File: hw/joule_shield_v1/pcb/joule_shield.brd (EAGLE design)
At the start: 160 x 100 mm, 18 parts, among them U2 BQ25892PWQFN-24

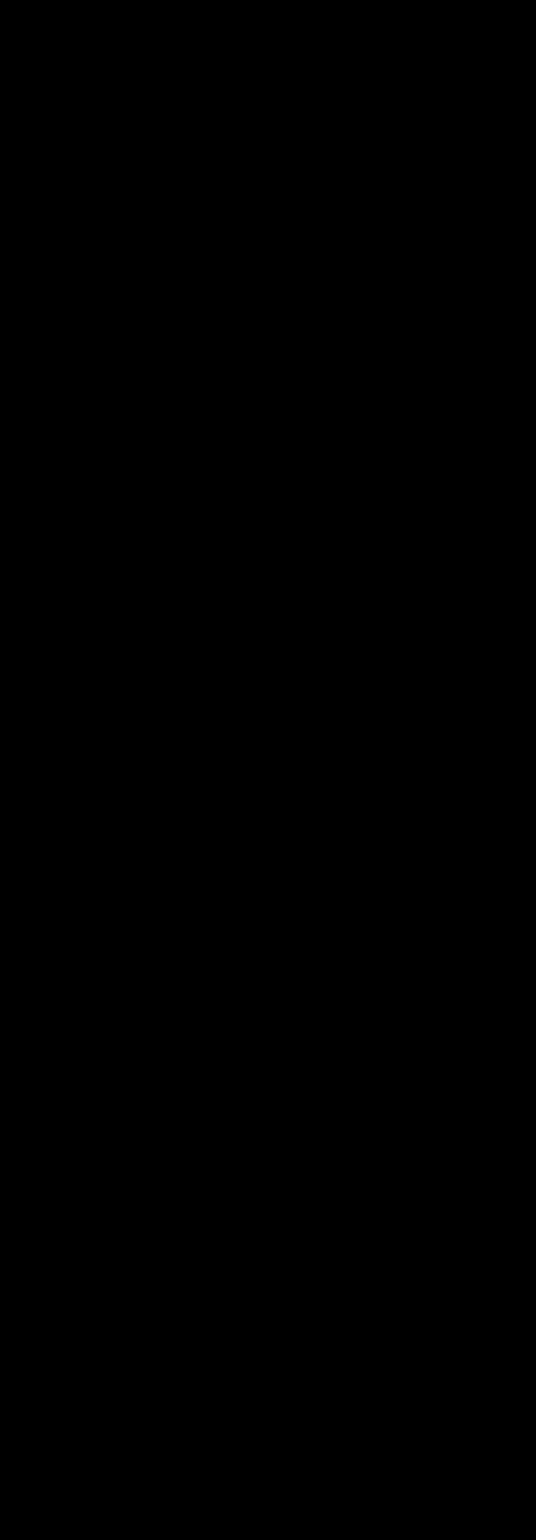
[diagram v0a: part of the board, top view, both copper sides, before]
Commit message: Schematic for 5V regulator.
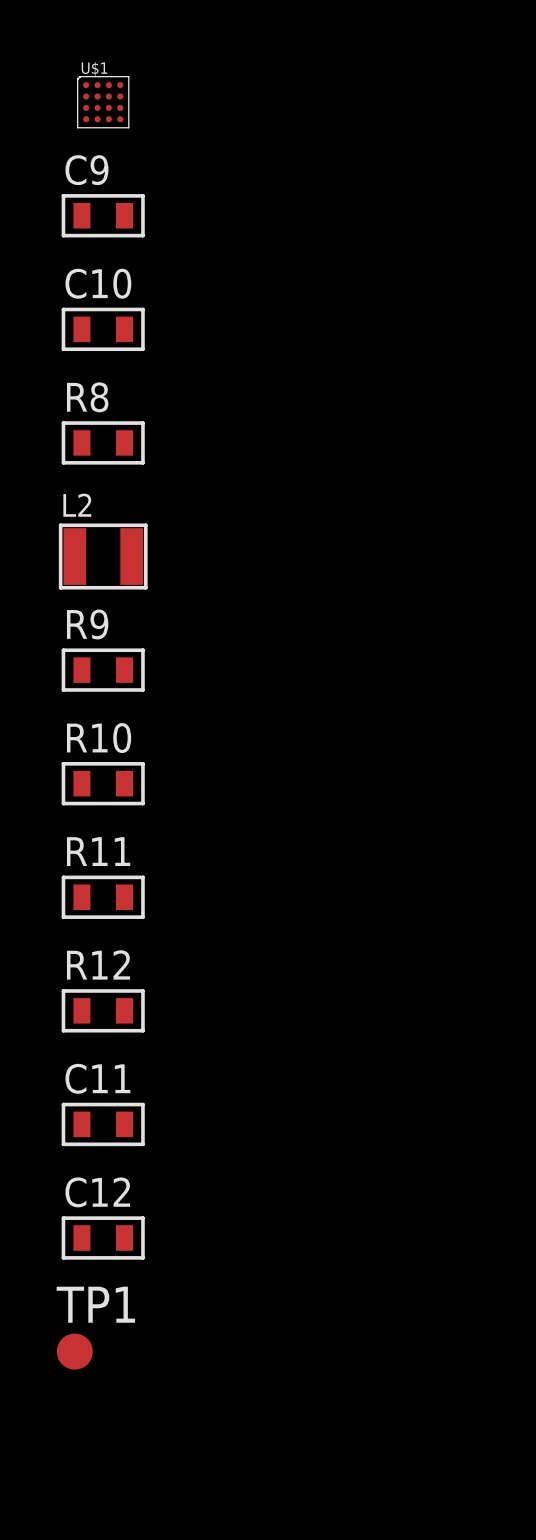
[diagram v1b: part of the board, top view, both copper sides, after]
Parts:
- added C10: 1nF, mf_passives:C0603
- added C11, C12: 22uF, mf_passives:C0603
- added C9: 10uF, mf_passives:C0603
- added L2: 470nH, joule_shield:DFE252010P
- added R10: 220k, mf_passives:R0603
- added R11: 1k, mf_passives:R0603
- added R12, R9: 100k, mf_passives:R0603
- added R8: 0, mf_passives:R0603
- added TP1: TPSQB1,27, testpad:B1,27
- added U$1: FAN8623WLCSP16, joule_shield:WLCSP16
- L1: value INDUCTORSPM4012 -> 1uH
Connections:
- new net +3V3: R9.P$1
- new net +5V: C11.P$1, C12.P$1, R12.P$1, U$1.B3, U$1.B4
- new net N$13: L2.1, U$1.C3, U$1.C4
- new net N$14: R10.P$1, R9.P$2, U$1.A1
- new net N$15: R11.P$2, U$1.C1
- new net N$18: R12.P$2, TP1.TP, U$1.A2
- new net N$7: R8.P$2, U$1.B1
- net +4.1V: now also C10.P$1, C9.P$1, L2.2, R11.P$1, R8.P$1, U$1.A3, U$1.A4
- net GND: now also C10.P$2, C11.P$2, C12.P$2, C9.P$2, R10.P$2, U$1.D1, U$1.D2, U$1.D3, U$1.D4

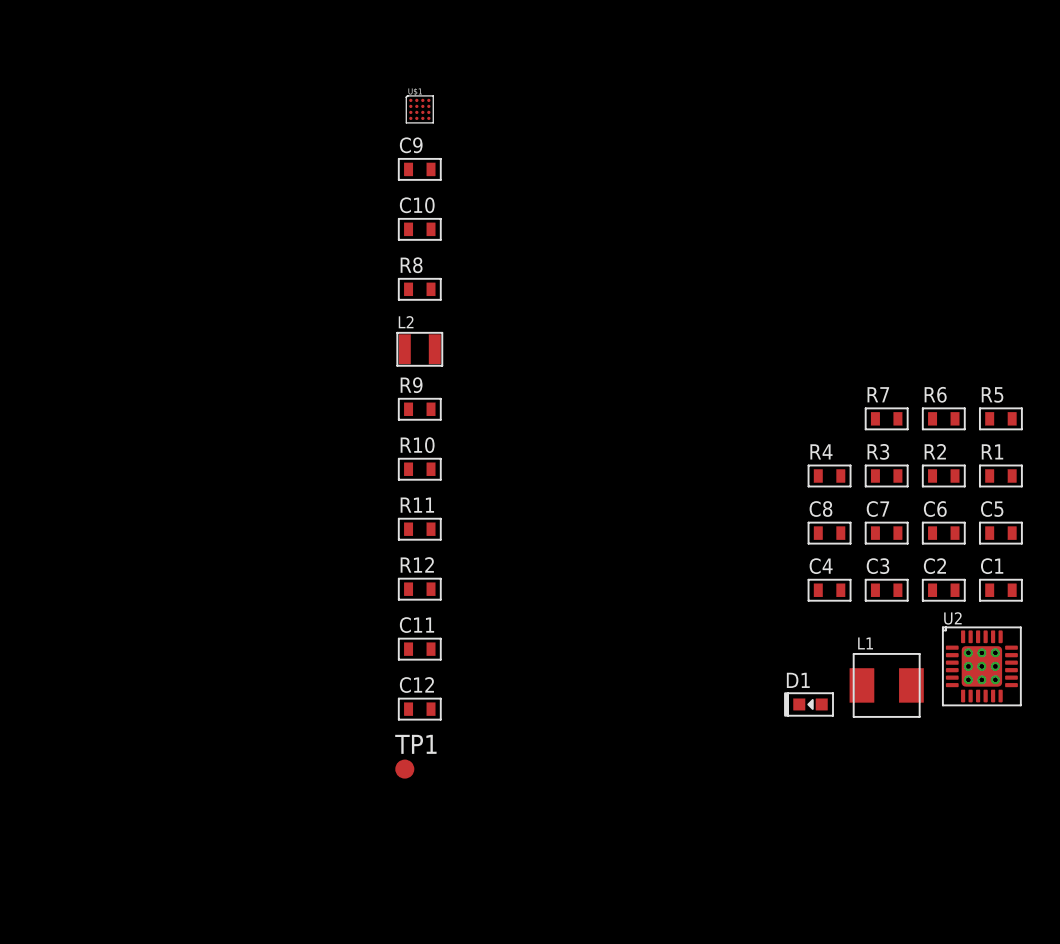
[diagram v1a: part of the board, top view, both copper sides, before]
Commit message: Schematic for 3.3V regulator.
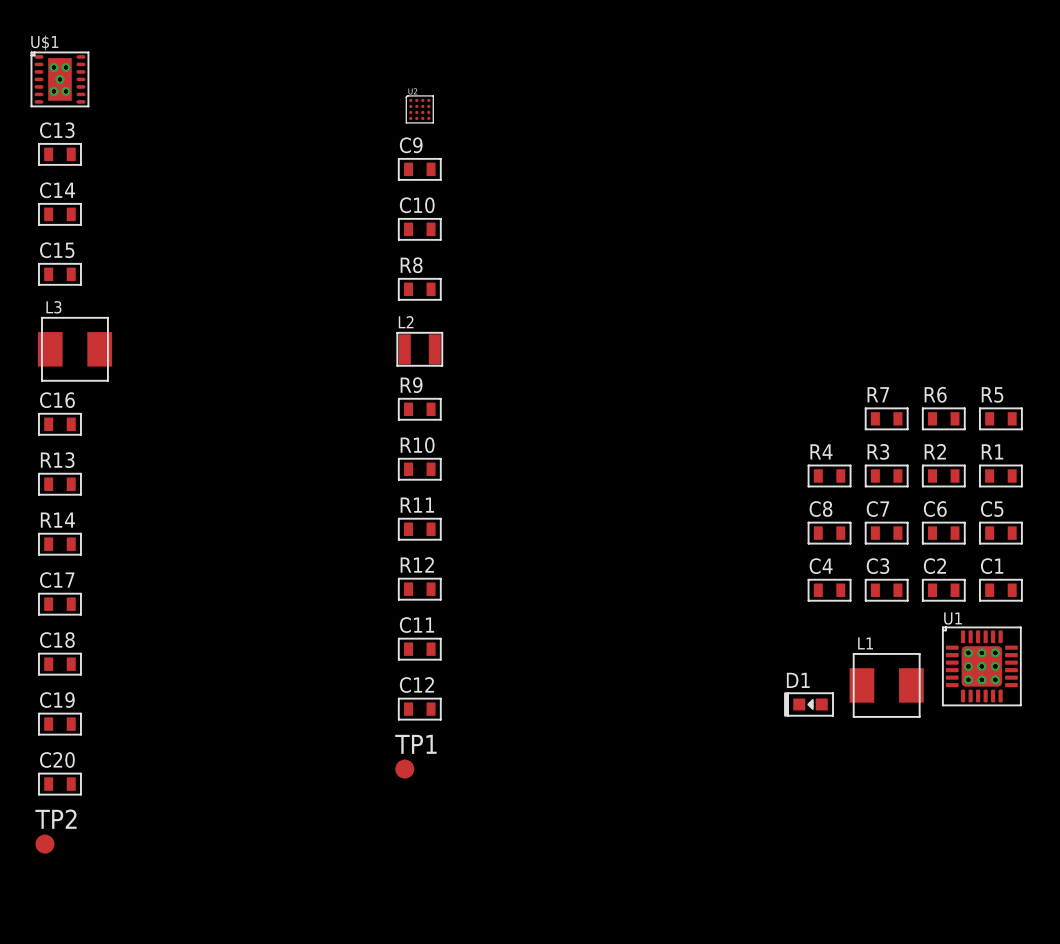
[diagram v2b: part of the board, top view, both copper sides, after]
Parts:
- added C13, C14: 10uF, mf_passives:C0603
- added C15, C20: 1uF, mf_passives:C0603
- added C16: 0.1uF, mf_passives:C0603
- added C17, C18, C19: 22uF, mf_passives:C0603
- added L3: 1uH, joule_shield:SPM4012
- added R13: 0, mf_passives:R0603
- added R14: 100k, mf_passives:R0603
- added TP2: TPSQB1,27, testpad:B1,27
- added U1: BQ25892PWQFN-24, joule_shield:PWQFN-24
- U$1: value FAN8623WLCSP16 -> TPS63201PVSON-14; device joule_shield:WLCSP16 -> joule_shield:PVSON-14
- U2: value BQ25892PWQFN-24 -> FAN8623WLCSP16; device joule_shield:PWQFN-24 -> joule_shield:WLCSP16
- moved U2 52.8 mm to (-54.0, 107.0)
- moved U$1 24.1 mm to (-78.0, 109.0)
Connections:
- new net N$16: L3.1, U$1.8, U$1.9
- new net N$17: L3.2, U$1.6, U$1.7
- new net N$19: C16.P$1, U$1.1
- new net N$20: R13.P$2, U$1.12
- new net N$21: R14.P$2, TP2.TP, U$1.14
- new net VDD: R13.P$1, R9.P$1
- net +3V3: now also C17.P$1, C18.P$1, C19.P$1, C20.P$1, R14.P$1, U$1.3, U$1.4, U$1.5; no longer R9.P$1
- net +4.1V: now also C13.P$1, C14.P$1, C15.P$1, U$1.10, U$1.11, U1.15, U1.16, U2.A3, U2.A4; no longer U$1.A3, U$1.A4, U2.15, U2.16
- net +5V: now also U2.B3, U2.B4; no longer U$1.B3, U$1.B4
- net GND: now also C13.P$2, C14.P$2, C15.P$2, C16.P$2, C17.P$2, C18.P$2, C19.P$2, C20.P$2, U$1.13, U$1.2, U$1.G0, U$1.G1, U$1.G2, U$1.G3, U$1.G4, U$1.G5, U1.17, U1.18, U1.G0, U1.G1, U1.G2, U1.G3, U1.G4, U1.G5, U1.G6, U1.G7, U1.G8, U1.G9, U2.D1, U2.D2, U2.D3, U2.D4; no longer U$1.D1, U$1.D2, U$1.D3, U$1.D4, U2.17, U2.18, U2.G0, U2.G1, U2.G2, U2.G3, U2.G4, U2.G5, U2.G6, U2.G7, U2.G8, U2.G9
- net I2C_0_SCL: now also U1.6; no longer U2.6
- net I2C_0_SDA: now also U1.5; no longer U2.5
- net N$10: now also U1.22; no longer U2.22
- net N$11: now also U1.21; no longer U2.21
- net N$12: now also U1.19, U1.20; no longer U2.19, U2.20
- net N$13: now also U2.C3, U2.C4; no longer U$1.C3, U$1.C4
- net N$14: now also U2.A1; no longer U$1.A1
- net N$15: now also U2.C1; no longer U$1.C1
- net N$18: now also U2.A2; no longer U$1.A2
- net N$2: now also U1.23; no longer U2.23
- net N$3: now also U1.10; no longer U2.10
- net N$4: now also U1.2; no longer U2.2
- net N$5: now also U1.8; no longer U2.8
- net N$6: now also U1.3; no longer U2.3
- net N$7: now also U2.B1; no longer U$1.B1
- net N$8: now also U1.11; no longer U2.11
- net N$9: now also U1.9; no longer U2.9
- net VCCIO: now also U1.1; no longer U2.1

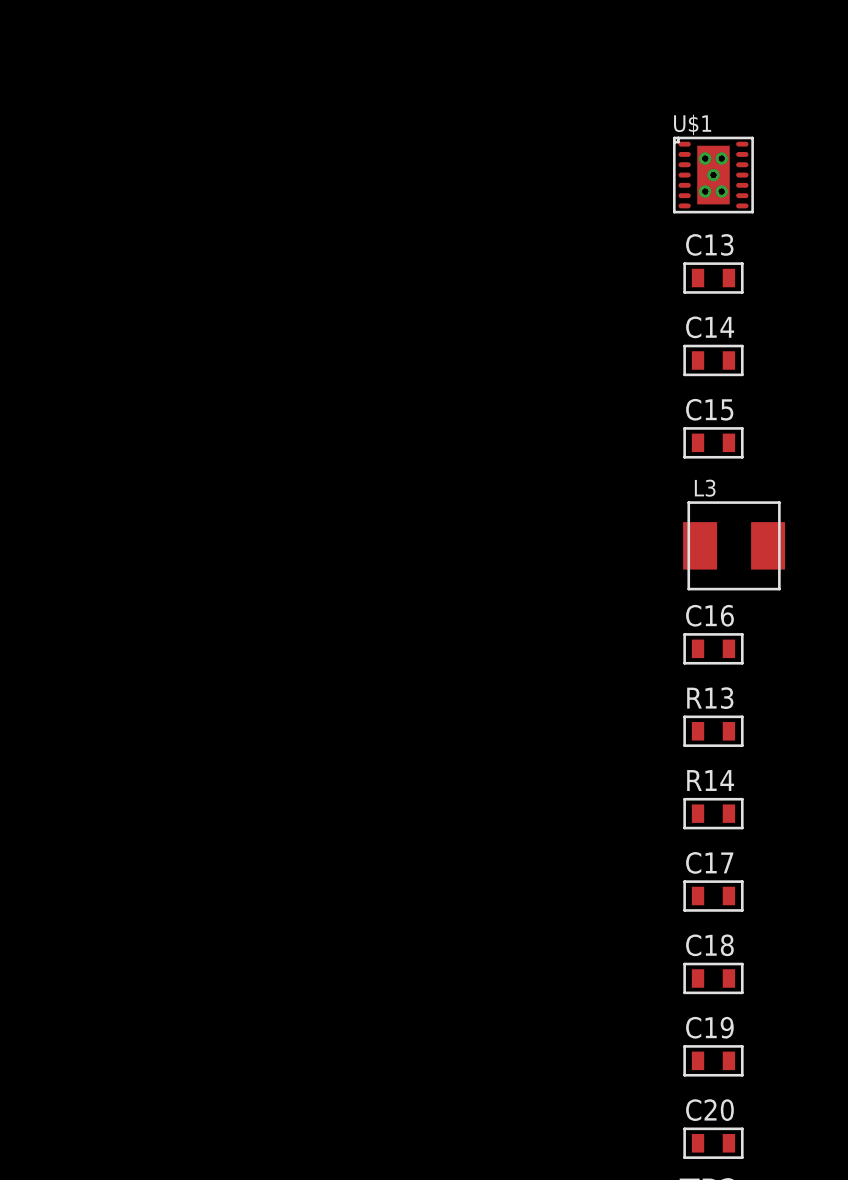
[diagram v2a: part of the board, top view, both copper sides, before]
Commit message: Schematic for 1.8V regulator.
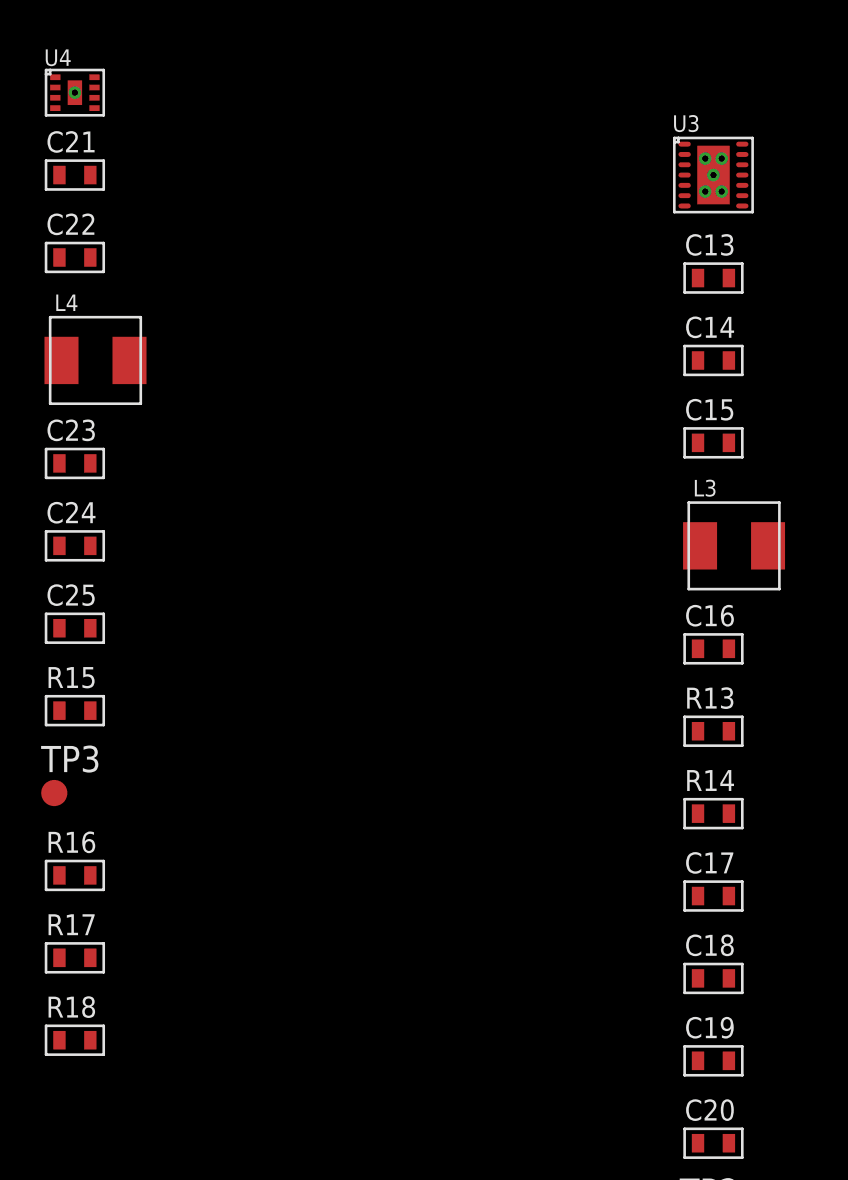
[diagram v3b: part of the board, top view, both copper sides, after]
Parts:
- added C21: 10uF, mf_passives:C0603
- added C22, C24, C25: 1uF, mf_passives:C0603
- added C23: 22uF, mf_passives:C0603
- added L4: 1uH, joule_shield:SPM4012
- added R15: 100k, mf_passives:R0603
- added R16: 110.0k 1%, mf_passives:R0603
- added R17: 36.5k 1%, mf_passives:R0603
- added R18: 0, mf_passives:R0603
- added TP3: TPSQB1,27, testpad:B1,27
- added U4: TLV62084PWSON-8, joule_shield:PWSON-8
- renumbered U$1 to U3
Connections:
- net +3V3 renamed V3P3V
- net +5V renamed V5P0V
- net VCCIO renamed VIN_CHRG
- net VDD renamed VDD3
- net VEE renamed VREGN
- new net N$23: L4.1, U4.7
- new net N$25: R15.P$2, TP3.TP, U4.6
- new net N$26: R16.P$2, R17.P$1, U4.4
- new net N$27: R18.P$2, U4.1
- new net V1P8V: C23.P$1, C24.P$1, C25.P$1, L4.2, R15.P$1, R16.P$1, U4.5
- new net VDD1: R18.P$1
- new net VSYS: C10.P$1, C13.P$1, C14.P$1, C15.P$1, C21.P$1, C22.P$1, C7.P$1, C8.P$1, C9.P$1, L1.2, L2.2, R11.P$1, R5.P$1, R8.P$1, U1.15, U1.16, U2.A3, U2.A4, U3.10, U3.11, U4.8
- net +4.1V: no longer C10.P$1, C13.P$1, C14.P$1, C15.P$1, C7.P$1, C8.P$1, C9.P$1, L1.2, L2.2, R11.P$1, R5.P$1, R8.P$1, U1.15, U1.16, U2.A3, U2.A4, U3.10, U3.11
- net GND: now also C21.P$2, C22.P$2, C23.P$2, C24.P$2, C25.P$2, R17.P$2, U4.2, U4.3, U4.G0, U4.G1
